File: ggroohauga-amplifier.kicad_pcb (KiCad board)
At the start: 2 copper layers, 95 x 31 mm, 9 parts

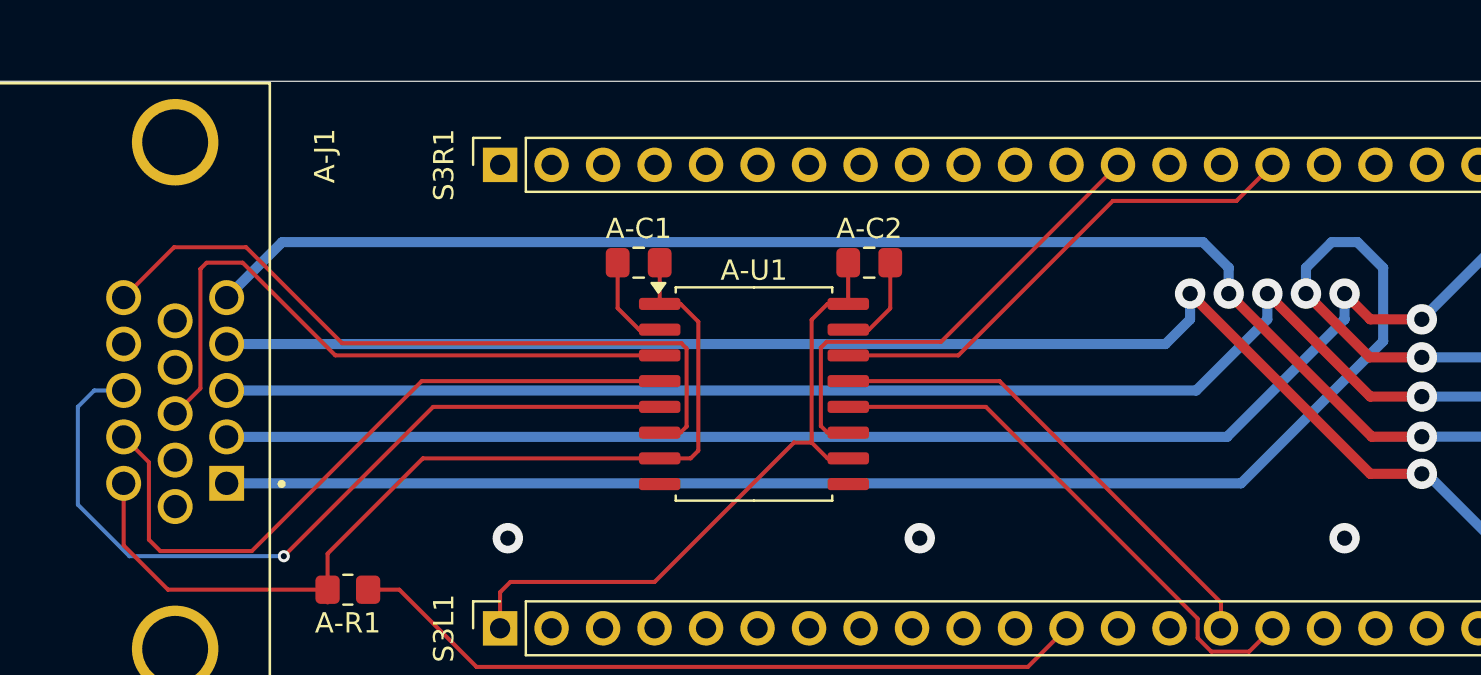
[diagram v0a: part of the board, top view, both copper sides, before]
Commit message: Add pull-up resistors to amplifier detect and RX inputs
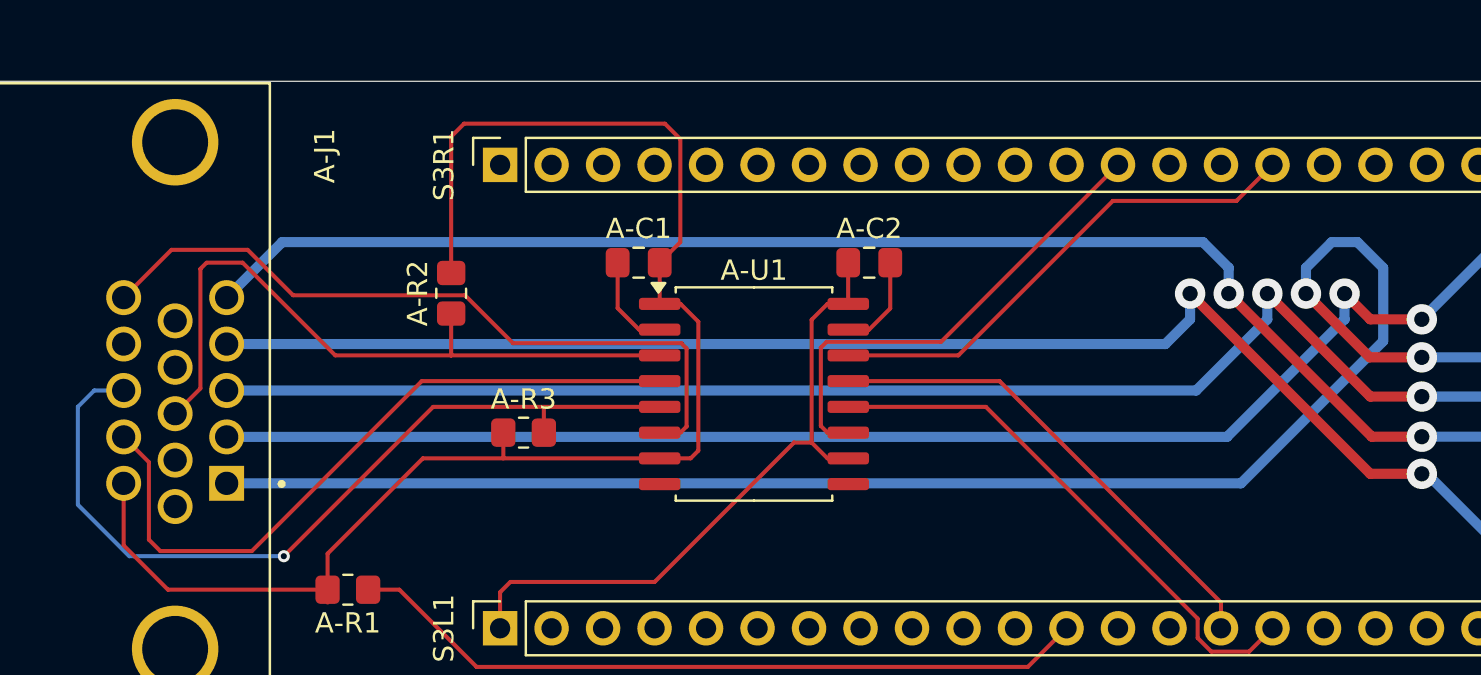
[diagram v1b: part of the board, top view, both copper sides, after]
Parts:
- added A-R2: 10kΩ, Resistor_SMD:R_0805_2012Metric_Pad1.20x1.40mm_HandSolder, F.Cu at (79.1, 60.9)
- added A-R3: 10kΩ, Resistor_SMD:R_0805_2012Metric_Pad1.20x1.40mm_HandSolder, F.Cu at (82.7, 67.8)
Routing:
- net /Common/AMP_POWER_IN: track 47.5 -> 73.9 mm
- net /Common/AMP_DETECT: track 32.3 -> 34.4 mm
- net /Common/AMP_RX: track 40.2 -> 41.5 mm
- net GND: vias 3 -> 0

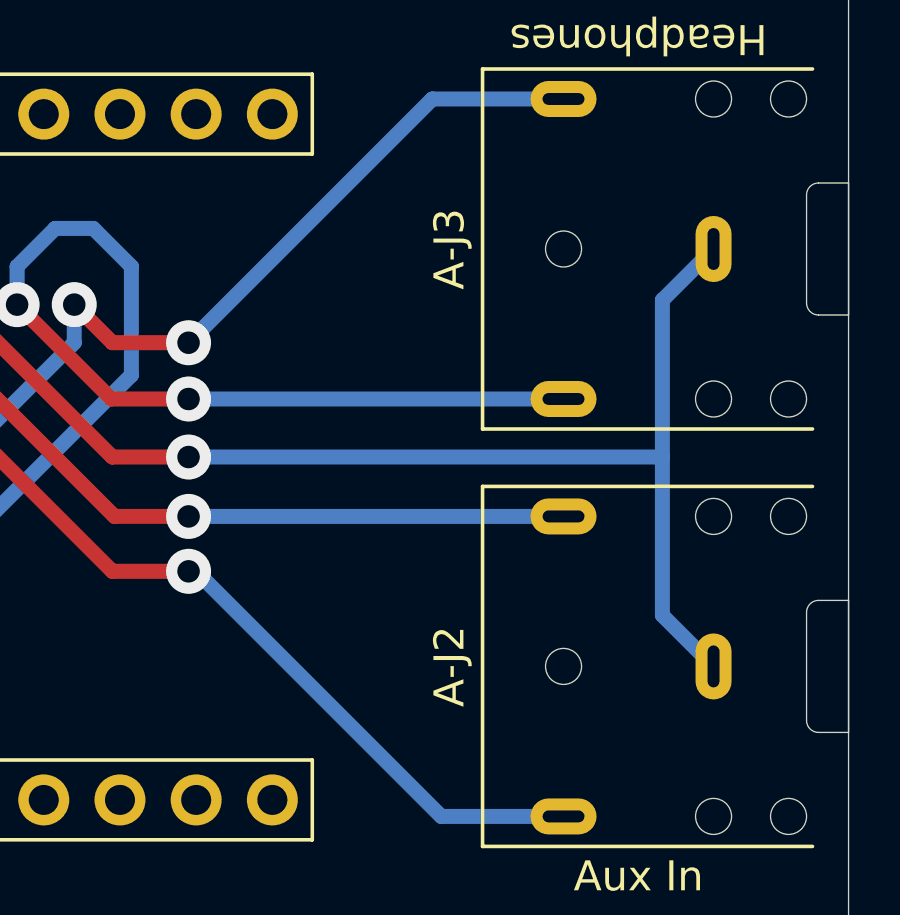
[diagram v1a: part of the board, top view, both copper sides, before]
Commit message: Fix component references for audio jacks
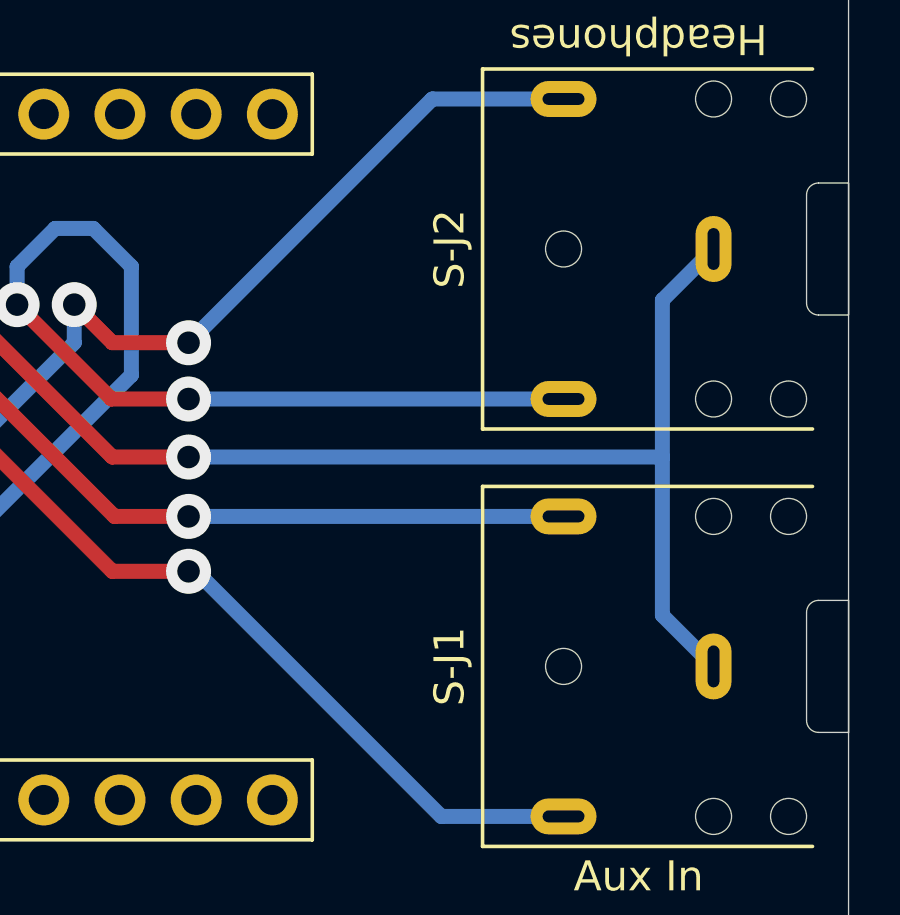
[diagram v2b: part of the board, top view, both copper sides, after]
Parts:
- renumbered A-J2 to S-J1, A-J3 to S-J2
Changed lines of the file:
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@@
 		(descr "TRS 3.5mm, horizontal, through-hole, https://www.cuidevices.com/product/resource/pdf/sj1-352xn.pdf")
 		(tags "TRS audio jack stereo horizontal")
-		(property "Reference" "A-J3"
+		(property "Reference" "S-J2"
 			(at 0 -8.8 90)
 			(layer "F.SilkS")
@@
 		(descr "TRS 3.5mm, horizontal, through-hole, https://www.cuidevices.com/product/resource/pdf/sj1-352xn.pdf")
 		(tags "TRS audio jack stereo horizontal")
-		(property "Reference" "A-J2"
+		(property "Reference" "S-J1"
 			(at 0 -8.8 90)
 			(layer "F.SilkS")

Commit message: Add "music with rocks in" image
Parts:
- added MUSICWITHROCKSIN: LOGO, LOGO, B.Cu at (81.3, 64.5)

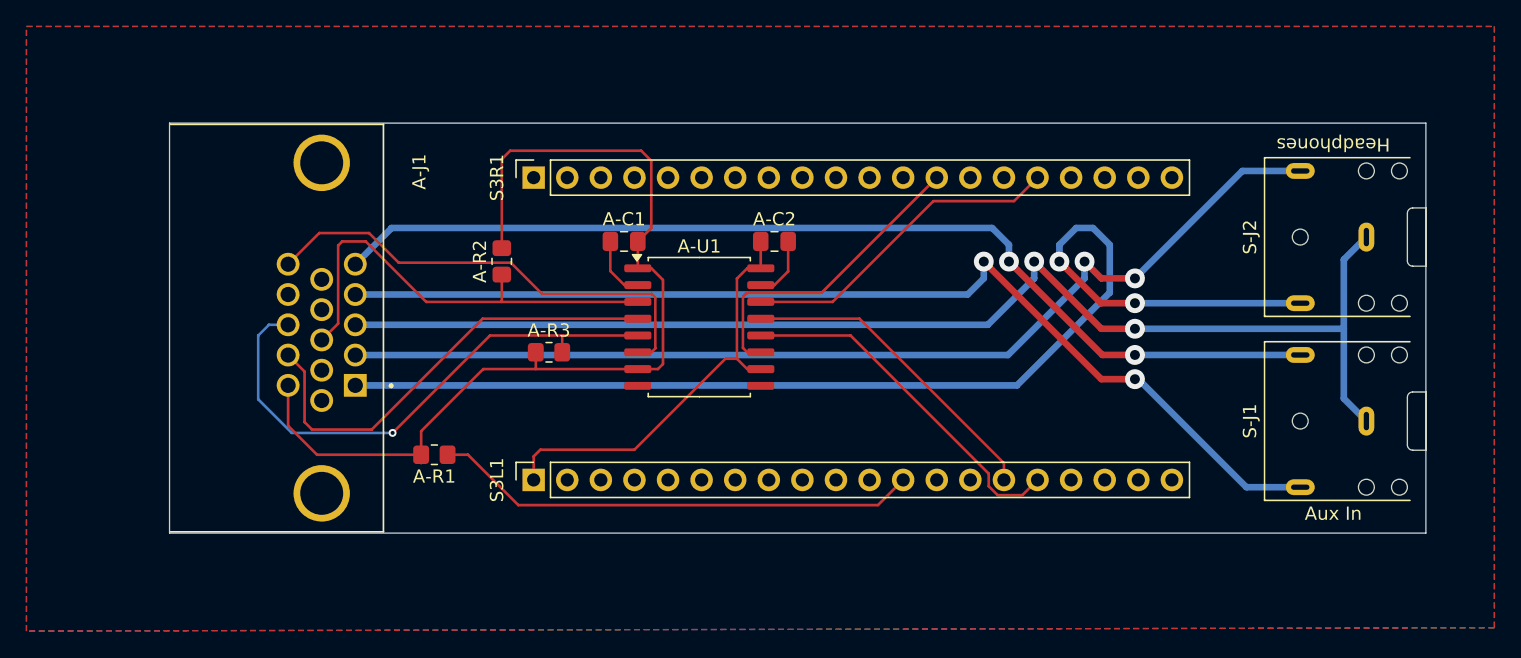
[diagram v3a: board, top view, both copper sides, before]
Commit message: Realign amplifier and bridge PCBs so that they match
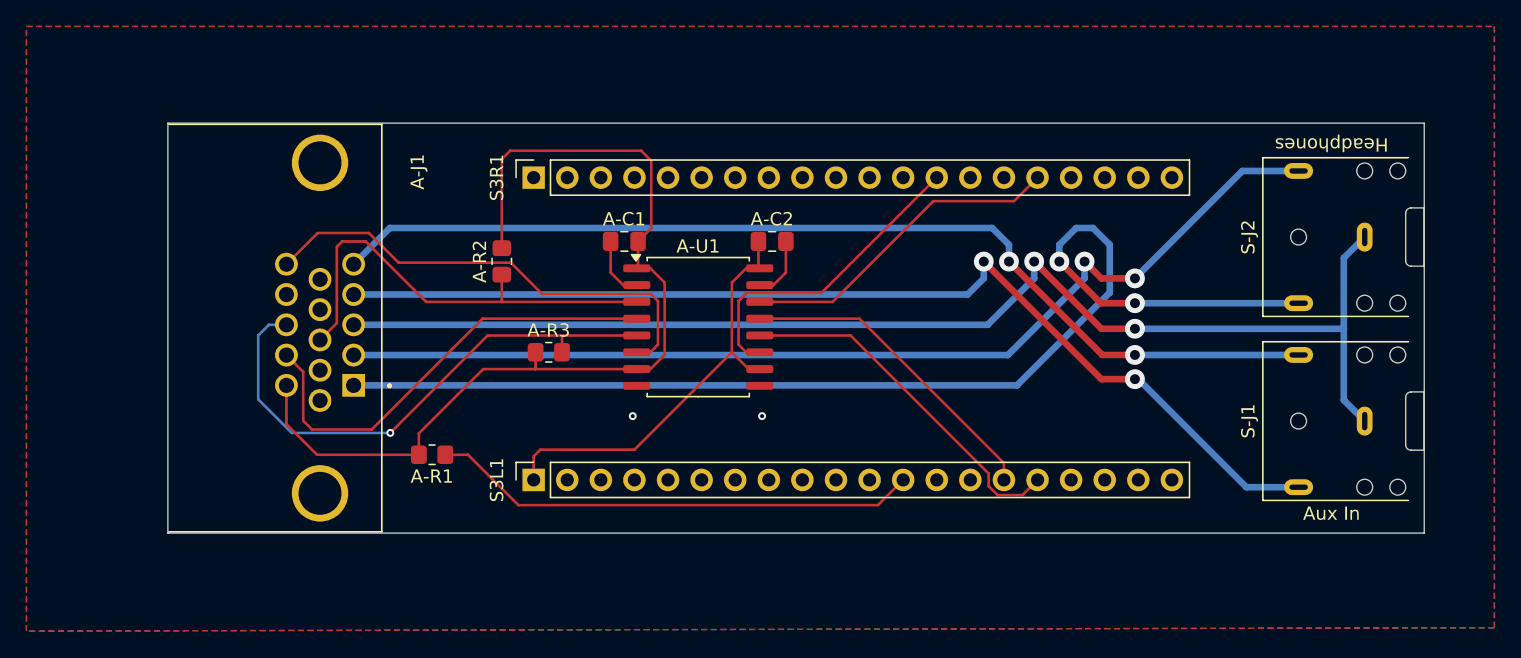
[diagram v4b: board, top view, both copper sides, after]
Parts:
- moved A-C2 0.17 mm to (99.6, 59.4)
- moved A-R1 0.17 mm to (73.9, 75.6)
- moved A-J1 0.13 mm to (65.4, 66.0)
- moved S-J1 0.13 mm to (144.4, 73.0)
- moved S-J2 0.13 mm to (144.4, 59.1)
- moved A-U1 0.08 mm to (94.0, 65.9)
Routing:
- net /Common/AMP_POWER_IN: track 73.9 -> 72.9 mm
- net +3.3V: track 32.6 -> 31.6 mm
- net GND: track 9.52 -> 10.5 mm, vias 0 -> 2

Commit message: Fix thin lines in image
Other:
- board text added: "https://github.com/nomis/ggroohauga-pcb (amplifier)"
- board text added: "urn:oid:1.3.6.1.4.1.39777.1.3.1.1.3"
- board text removed: "urn:oid:1.3.6.1.4.1.39777.1.3.1.1.3 https://github.com/nomis/ggroohauga-pcb (amplifier)"

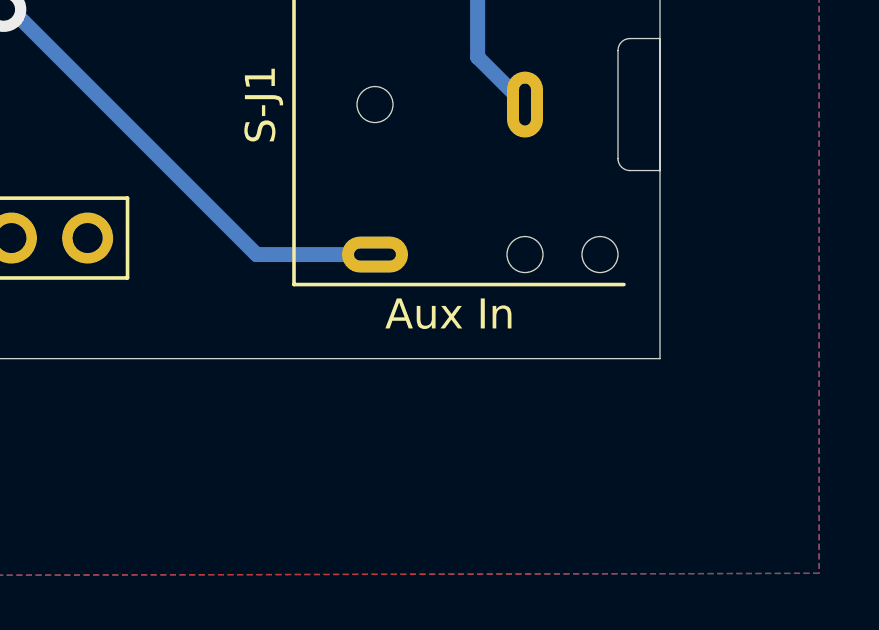
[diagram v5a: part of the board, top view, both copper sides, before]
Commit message: Rename "Aux In" to "Aux Input" and document 3.5mm audio sockets
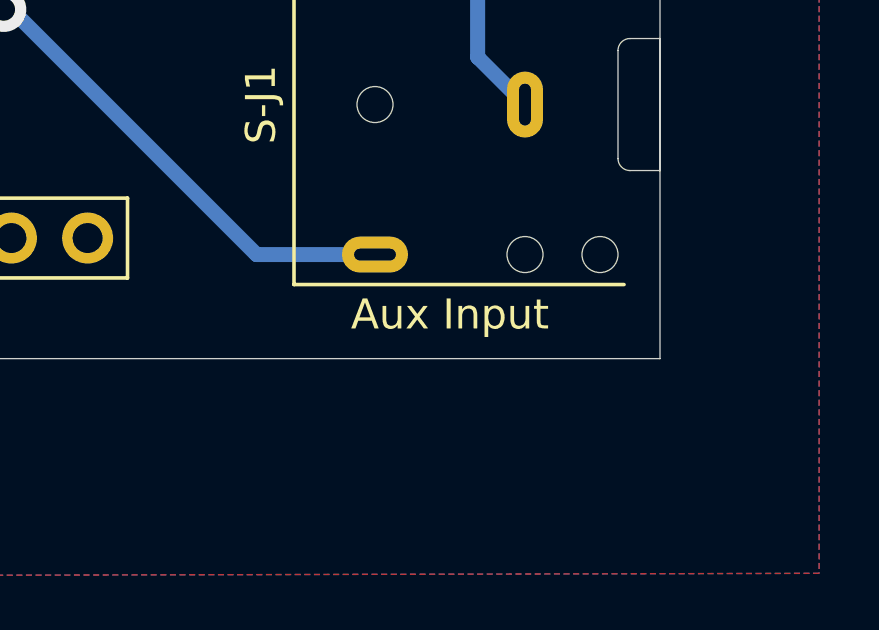
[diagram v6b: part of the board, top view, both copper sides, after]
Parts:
- S-J1: value Aux In -> Aux Input
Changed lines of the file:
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@@
 			)
 		)
-		(property "Value" "Aux In"
+		(property "Value" "Aux Input"
 			(at -7 -2.5 0)
 			(unlocked yes)
